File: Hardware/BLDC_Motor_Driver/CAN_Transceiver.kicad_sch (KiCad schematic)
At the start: 0 parts

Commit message: Add Selection of CAN IC and arrange the sheet of buck converter
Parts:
- added R10, R9: R, symbol Device:R
- added U2: TCAN334DR, BLDC_Motor_Driver_Components_Footprint:SOIC127P599X175-8N, symbol TCAN334DR:TCAN334DR
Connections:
- new net: R9.2, U2.1 (TXD)
- new net: R10.2, U2.4 (RXD)
- new net +3.3V: U2.3 (VCC)
- new net GND: U2.2 (GND)
- new net RXD: R10.1
- new net TXD: R9.1

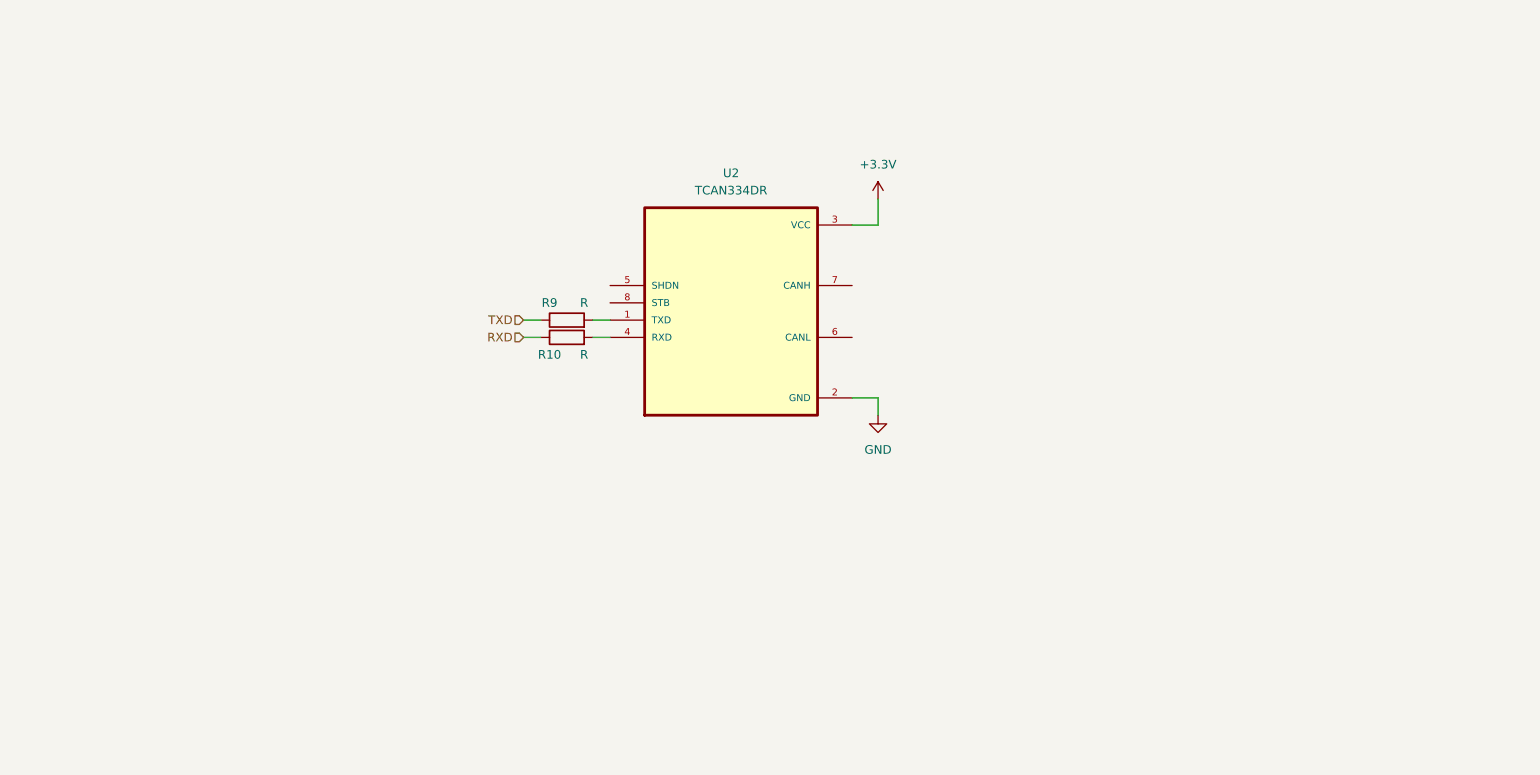
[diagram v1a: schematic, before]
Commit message: Complete CAN IC sheet
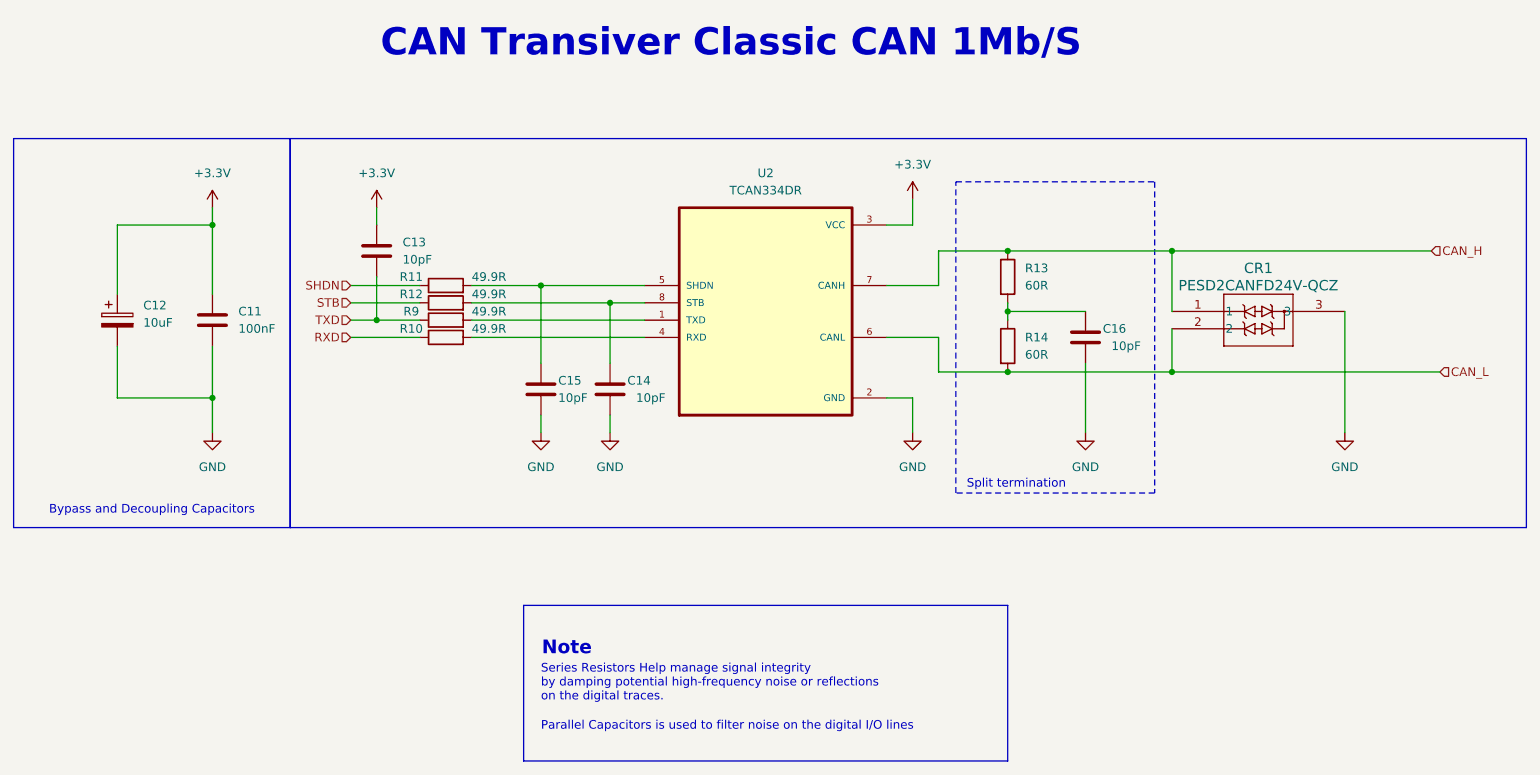
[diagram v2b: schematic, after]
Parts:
- added C11: 100nF, Capacitor_SMD:C_0603_1608Metric, symbol Device:C
- added C12: 10uF, Capacitor_Tantalum_SMD:CP_EIA-3216-18_Kemet-A, symbol Device:C_Polarized
- added C13, C14, C15, C16: 10pF, Capacitor_SMD:C_0603_1608Metric, symbol Device:C
- added CR1: PESD2CANFD24V-QCZ, BLDC_Motor_Driver_Components_Footprint:DFN1412D-3_SOT8009_NEX, symbol PESD2CANFD27V-QCZ:PESD2CANFD24V-QCZ
- added R11, R12: 49.9R, Resistor_SMD:R_0805_2012Metric, symbol Device:R
- added R13, R14: 60R, Capacitor_SMD:C_0603_1608Metric, symbol Device:R
- R10, R9: value R -> 49.9R; footprint (none) -> Resistor_SMD:R_0805_2012Metric; Assembled (none) -> Yes; LCSC_PN (none) -> C269747; MP (none) -> RMC080549.91%N
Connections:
- net +3.3V: now also C11.2, C12.1, C13.1
- net GND: now also C11.1, C12.2, C14.2, C15.2, C16.2, CR1.3
- net TXD: now also C13.2
- net at U2.5 (SHDN): now also C15.1, R11.2
- net CAN_L: now reaches U2.6 (CANL)
- net CAN_L: now also CR1.2, R14.2
- net CAN_H: now reaches U2.7 (CANH)
- net CAN_H: now also CR1.1, R13.1
- net at U2.8 (STB): now also C14.1, R12.2
- new net: C16.1, R13.2, R14.1
- new net SHDN: R11.1
- new net STB: R12.1
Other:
- note added: "Bypass and Decoupling Capacitors"
- note added: "CAN Transiver Classic CAN 1Mb/S"
- note added: "Note"
- note added: "Parallel Capacitors is used to filter noise on the digital I/O lines"
- note added: "Series Resistors Help manage signal integrity by damping potential high-frequency noise or reflections on the digital traces."
- note added: "Split termination"
- title: (none) -> ${Project_Name}
- moved on the sheet: R9, U2

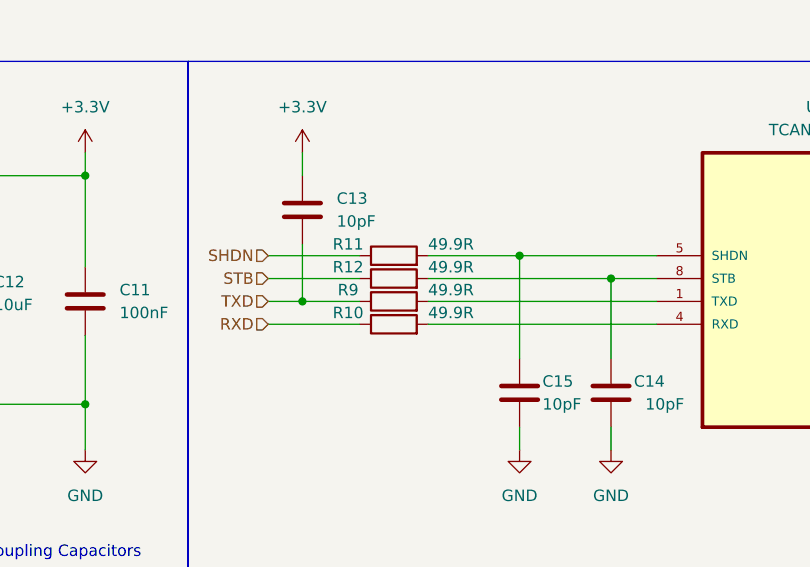
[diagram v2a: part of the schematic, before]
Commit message: Edit the value of series resistor to 33R instead of 49.9R
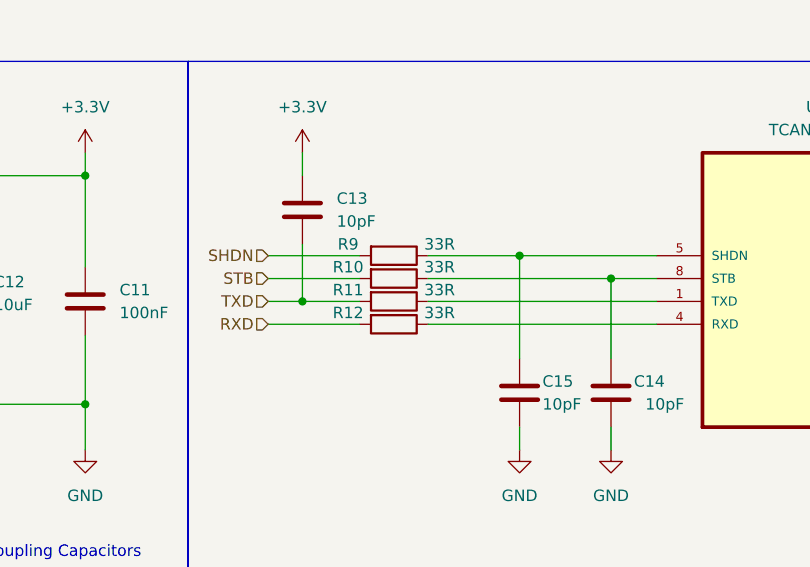
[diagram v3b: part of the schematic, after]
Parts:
- R10, R11, R12, R9: value 49.9R -> 33R; footprint Resistor_SMD:R_0805_2012Metric -> Resistor_SMD:R_0603_1608Metric; LCSC_PN C269747 -> C108661; MP RMC080549.91%N -> RC0603FR-0733RL
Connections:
- net RXD: now also R12.2; no longer R10.1
- net SHDN: now also R9.2; no longer R11.1
- net STB: now also R10.2; no longer R12.1
- net TXD: now also R11.2; no longer R9.1
- net at U2.1 (TXD): now also R11.1; no longer R9.2
- net at U2.4 (RXD): now also R12.1; no longer R10.2
- net at C15.1, U2.5 (SHDN): now also R9.1; no longer R11.2
- net at C14.1, U2.8 (STB): now also R10.1; no longer R12.2
